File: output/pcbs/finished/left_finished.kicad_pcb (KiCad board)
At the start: 2 copper layers, 142.5 x 107.8 mm, 97 parts

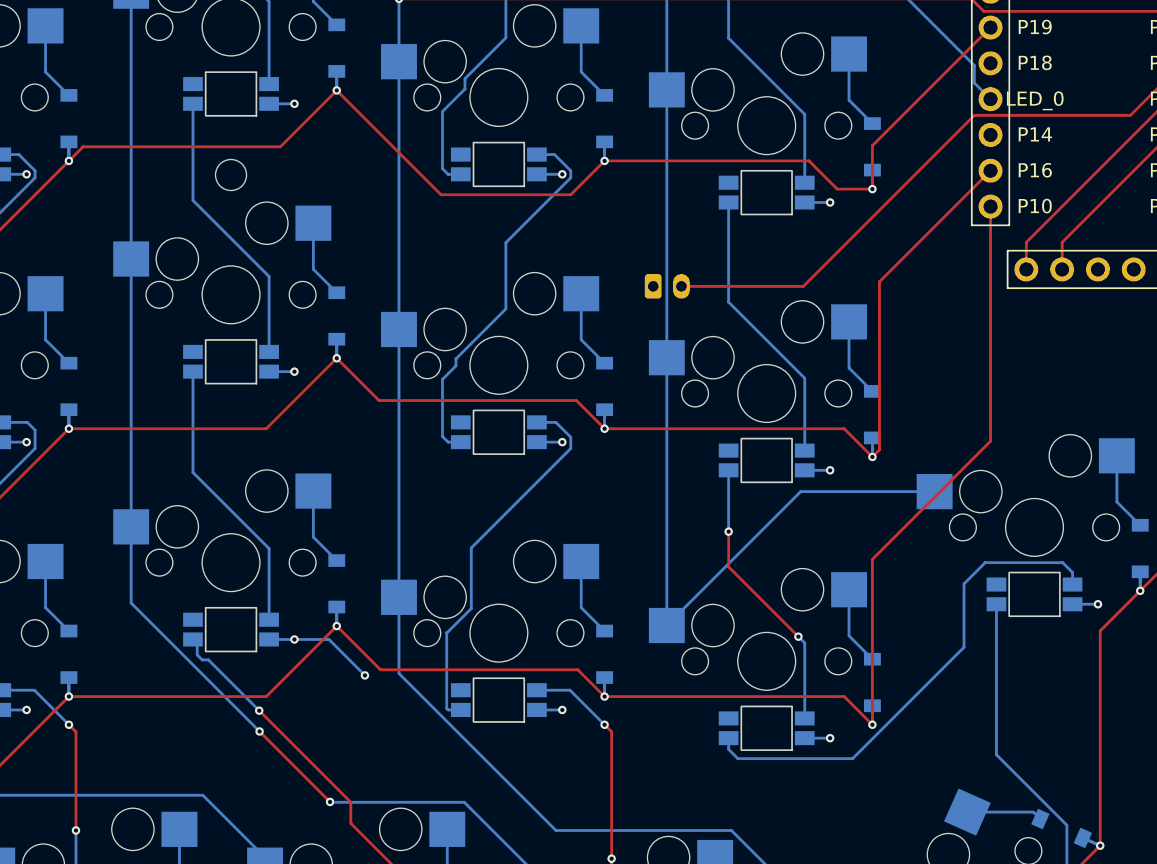
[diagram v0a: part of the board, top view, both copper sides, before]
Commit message: Add JLC text to board
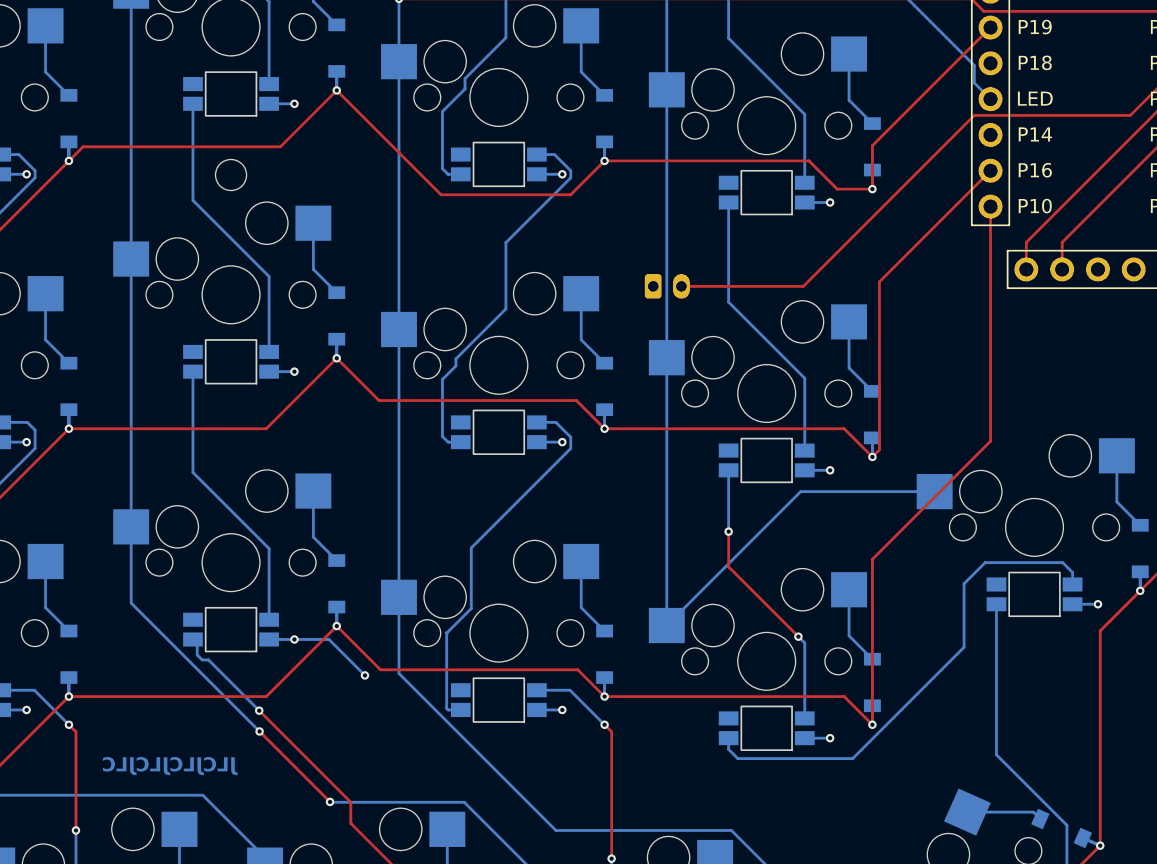
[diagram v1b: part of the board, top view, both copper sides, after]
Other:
- board text added: "JLCJLCJLCJLC"
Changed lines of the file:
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@@
 			)
 		)
-		(fp_text user "LED_0"
+		(fp_text user "LED"
 			(at -4.47 7.62 0)
 			(layer "F.SilkS")
@@
 		(layer "Edge.Cuts")
 	)
+	(gr_text "JLCJLCJLCJLC"
+		(at 200.61 172.34 0)
+		(layer "B.Cu")
+		(effects
+			(font
+				(size 1 1)
+				(thickness 0.1)
+				(bold yes)
+			)
+			(justify mirror)
+		)
+	)
 	(gr_text "Jokkess"
